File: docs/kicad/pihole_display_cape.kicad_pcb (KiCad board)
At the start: 2 copper layers, 55 x 28 mm, 3 parts, among them J1 P9_1-20, J2 P8_1-20, J3 DISP_1x8

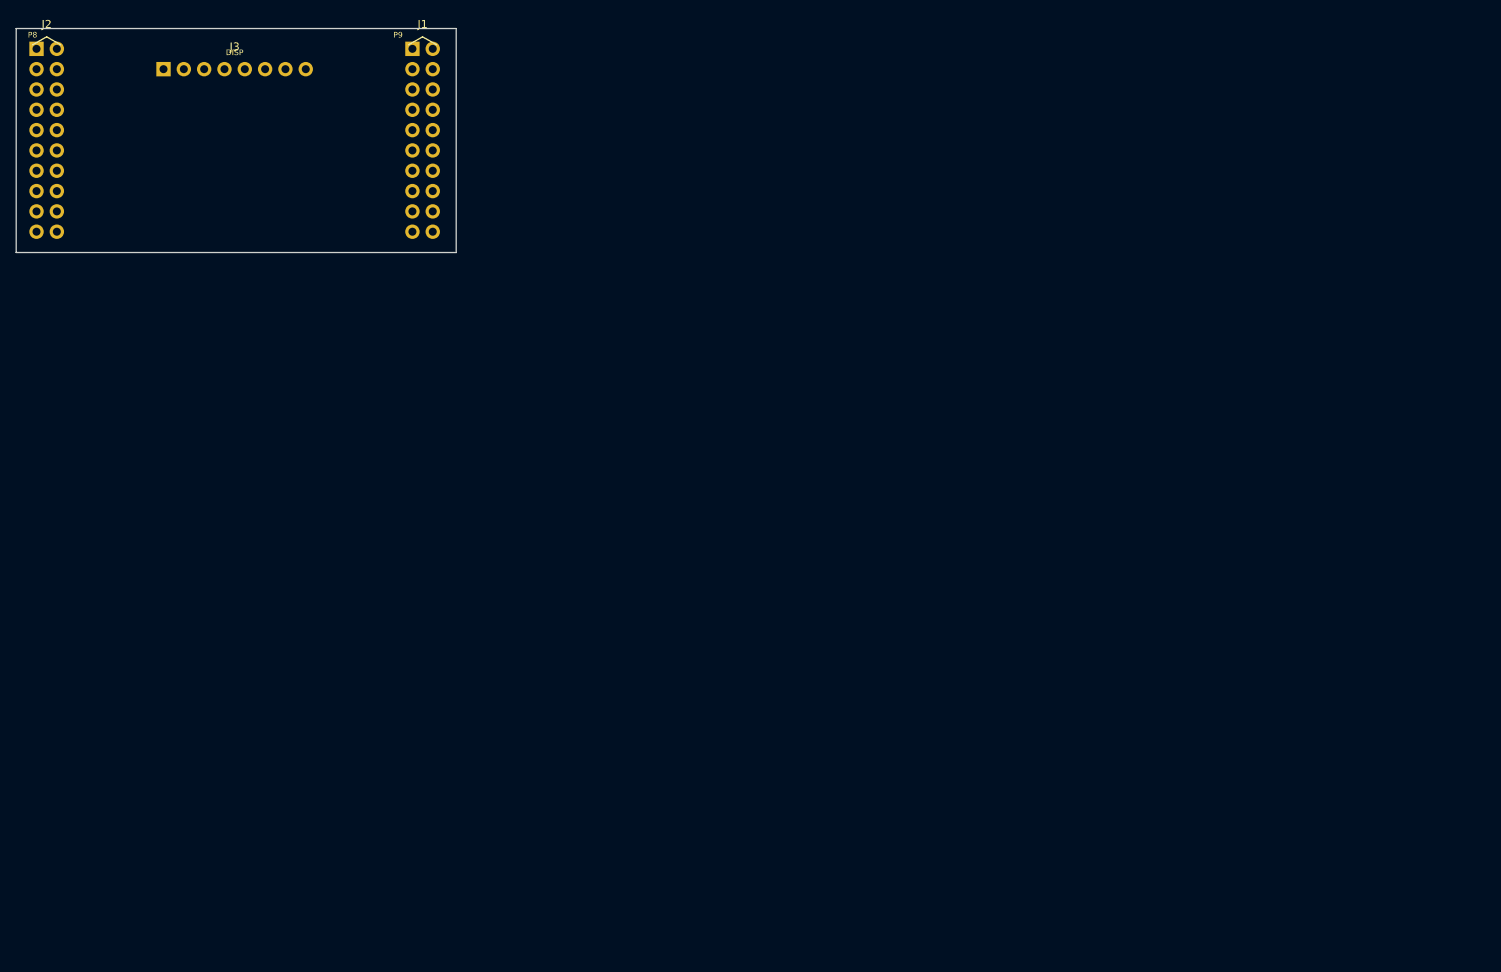
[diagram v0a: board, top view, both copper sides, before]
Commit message: Add screen lock feature and improve button handling
- Implemented a screen lock feature that can be toggled via the menu.
- Added a hold action for the back button to wake the display when locked.
- Enhanced button handler to support hold events and prevent multiple triggers.
- Updated display manager to show hints with pixel arrows instead of text.
- Refactored code for better readability and maintainability.
- Added versioning support for the application.
- Updated installation script to check for unbound-control and provide guidance.
- Added new mockup images for UI updates.
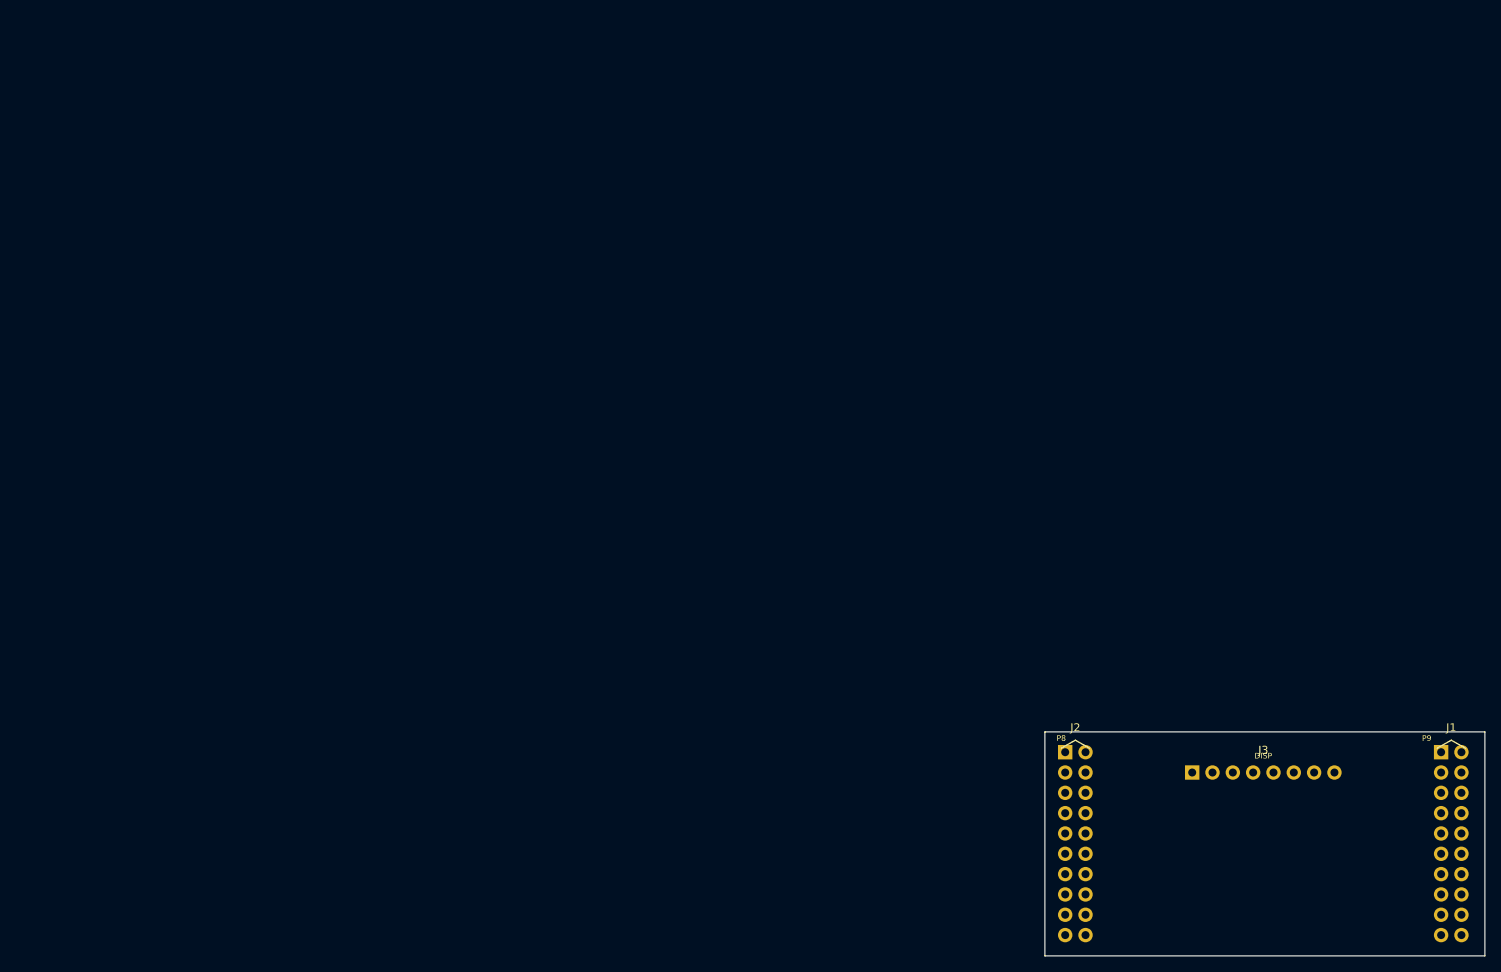
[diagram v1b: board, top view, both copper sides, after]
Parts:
- moved J2 155.8 mm to (132.4, 101.9)
- moved J1 155.8 mm to (179.4, 101.9)
- moved J3 155.8 mm to (155.9, 93.0)
